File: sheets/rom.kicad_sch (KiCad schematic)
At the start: 3 parts, among them U34 NEO-E0, U35 74LS259, U36 27C1024

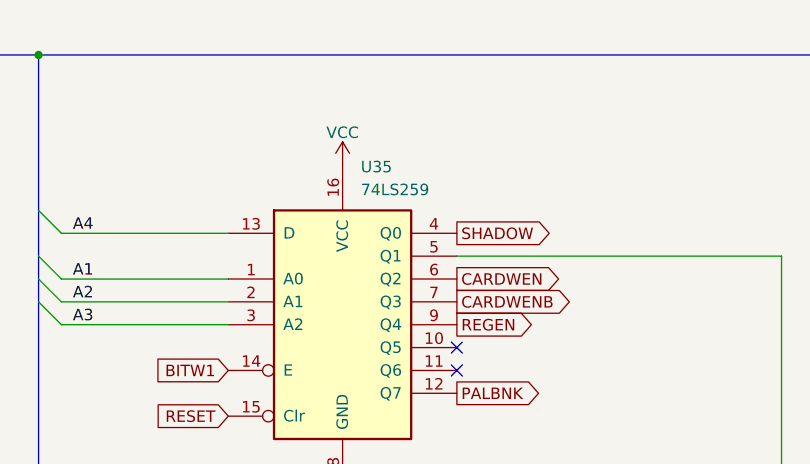
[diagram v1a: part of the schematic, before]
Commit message: More silkscreen tidy up, adding mouser components to BOM
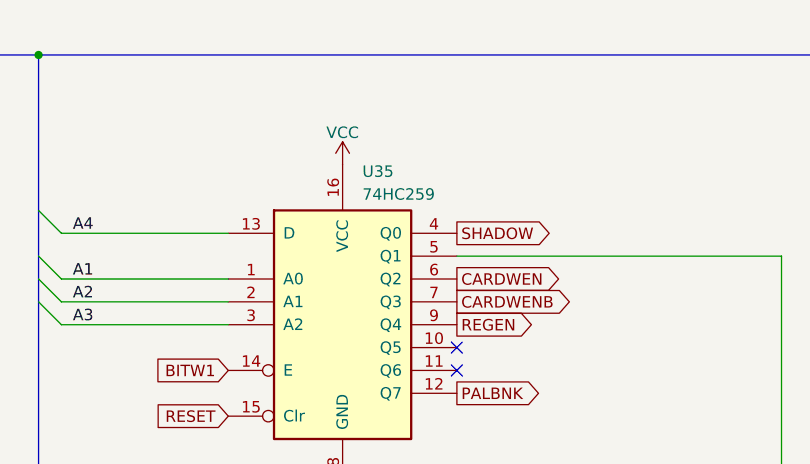
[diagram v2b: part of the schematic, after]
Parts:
- U35: value 74LS259 -> 74HC259
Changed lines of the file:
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@@
   (symbol (lib_id "74xx:74LS259") (at 156.21 93.218 0) (unit 1)
     (in_bom yes) (on_board yes) (dnp no) (fields_autoplaced)
-    (property "Reference" "U35" (at 158.2294 75.692 0)
+    (property "Reference" "U35" (at 158.4041 76.2 0)
       (effects (font (size 1.27 1.27)) (justify left))
     )
-    (property "Value" "74LS259" (at 158.2294 78.232 0)
+    (property "Value" "74HC259" (at 158.4041 78.74 0)
       (effects (font (size 1.27 1.27)) (justify left))
     )

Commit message: Little tweaks to silkscreen Updated BOM with mouser parts
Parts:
- U34, U36: Comment (none) -> Use Original
- U35: Mouser (none) -> 595-SN74HC259N
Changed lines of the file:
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@@
     (title "NeoGeo AES 3-5")
     (date "2023-08-27")
-    (rev "BF1.1")
+    (rev "BF1.2")
     (company "SNK")
     (comment 3 "https://github.com/Board-Folk")
@@
     )
     (property "Mouser" "" (at 157.48 152.654 0)
+      (effects (font (size 1.27 1.27)) hide)
+    )
+    (property "Alternative" "" (at 157.48 152.654 0)
+      (effects (font (size 1.27 1.27)) hide)
+    )
+    (property "Comment" "Use Original" (at 157.48 152.654 0)
       (effects (font (size 1.27 1.27)) hide)
     )
@@
       (effects (font (size 1.27 1.27)) hide)
     )
-    (property "Mouser" "" (at 156.21 93.218 0)
+    (property "Mouser" "595-SN74HC259N" (at 156.21 93.218 0)
+      (effects (font (size 1.27 1.27)) hide)
+    )
+    (property "Alternative" "" (at 156.21 93.218 0)
       (effects (font (size 1.27 1.27)) hide)
     )
@@
       (effects (font (size 1.27 1.27)) hide)
     )
+    (property "Comment" "Use Original" (at 253.746 136.144 0)
+      (effects (font (size 1.27 1.27)) hide)
+    )
+    (property "Alternative" "" (at 253.746 136.144 0)
+      (effects (font (size 1.27 1.27)) hide)
+    )
